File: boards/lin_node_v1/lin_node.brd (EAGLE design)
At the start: 50.1 x 38.4 mm, 27 parts, among them J1 AVR_SPI_PRG_6NS, U1 ATtiny167, U2 MCP2025, U3 VNQ5160K

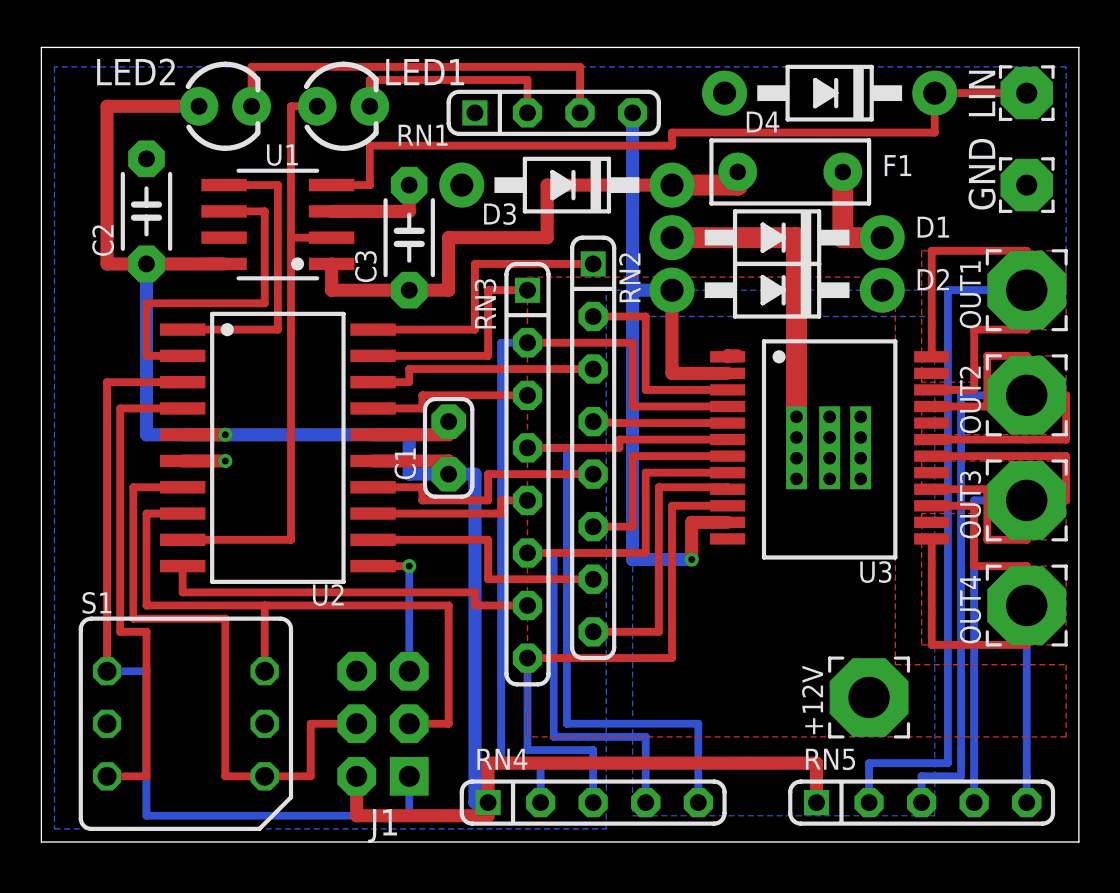
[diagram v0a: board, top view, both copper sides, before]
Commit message: Update to current sample boards
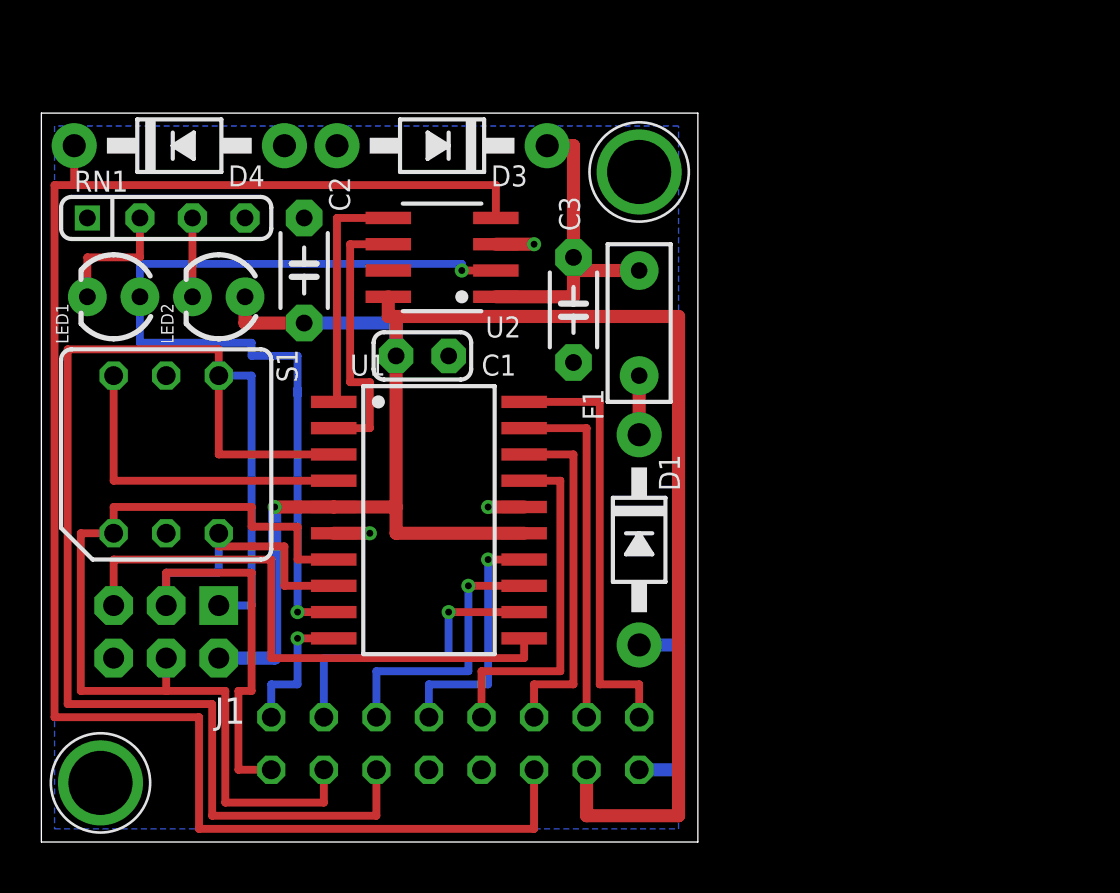
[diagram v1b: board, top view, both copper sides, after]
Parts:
- removed +12V, OUT1, OUT2, OUT3, OUT4: WIREPADTH-2.0MM, custom:WIREPAD-TH-2.0MM
- removed D2: 1N4004, custom:DO41-10
- removed GND, LIN: WIREPAD2,54/1,0, custom:2,54/1,0
- removed RN2, RN3: 10K, custom:SIL8
- removed RN4, RN5: 10K, custom:SIL5
- removed U3: VNQ5160K, custom:POWERSSO24
- added SV1: (no value), custom:FE08-2
- added U$1, U$2: MOUNT-HOLE3.1MM, custom:MOUNT-HOLE3.1
- moved D4 31.5 mm to (6.67, 33.7), turned to 0 degrees
- moved RN1 19.4 mm to (6.03, 30.2)
- moved D1 16.1 mm to (28.9, 14.6), turned to 270 degrees
- moved LED1 14.4 mm to (3.49, 26.4), turned to 180 degrees
- moved S1 13.1 mm to (6.03, 18.7), turned to 270 degrees
- moved J1 11.4 mm to (6.03, 10.2), turned to 180 degrees
- moved F1 10.3 mm to (28.9, 25.1), turned to 270 degrees
- moved LED2 9.21 mm to (8.57, 26.4), turned to 180 degrees
- moved C3 8.67 mm to (25.7, 25.7), turned to 270 degrees
- moved C2 8.14 mm to (12.7, 27.6)
- moved U1 8.09 mm to (18.7, 15.6)
- moved U2 8.09 mm to (19.4, 28.3)
- moved D3 6.33 mm to (19.4, 33.7)
- moved C1 4.62 mm to (18.4, 23.5), turned to 0 degrees
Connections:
- removed net N$1: D4.C, LIN.1, U2.4
- removed net N$10: RN3.2, RN4.2, U3.4
- removed net N$11: RN2.2, U3.3
- removed net N$12: RN2.8, U3.9
- removed net N$13: RN2.6, U3.7
- removed net N$14: RN2.4, U3.5
- removed net N$6: RN3.8, RN4.3, U3.10
- removed net N$7: RN3.6, RN4.4, U3.8
- removed net N$8: D2.A, RN1.4, U3.11, U3.2
- removed net N$9: RN3.4, RN4.5, U3.6
- removed net OUT1: RN2.1, U1.20
- removed net OUT2: RN2.3, U1.18
- removed net OUT3: RN2.5, U1.14
- removed net OUT4: RN2.7, U1.12
- removed net OUTPUT1: OUT1.1, RN5.2, U3.22, U3.23, U3.24
- removed net OUTPUT2: OUT2.1, RN5.3, U3.19, U3.20, U3.21
- removed net OUTPUT3: OUT3.1, RN5.4, U3.16, U3.17, U3.18
- removed net OUTPUT4: OUT4.1, RN5.5, U3.13, U3.14, U3.15
- removed net STATUS1: RN3.1, U1.19
- removed net STATUS2: RN3.3, U1.17
- removed net STATUS3: RN3.5, U1.13
- removed net STATUS4: RN3.7, U1.10
- new net LIN: D4.C, SV1.6, U2.4
- new net P0/SDA: SV1.1, U1.20
- new net P1: SV1.3, U1.19
- new net P2/SCL: SV1.5, U1.18
- new net P3: SV1.7, U1.17
- new net P4: SV1.9, U1.14
- new net P5/ADC8: SV1.11, U1.13
- new net P6/ADC9: SV1.13, U1.12
- new net P7/ADC7: SV1.15, U1.10
- net +12V: now also SV1.2; no longer +12V.1, U3.1, U3.12, U3.P$1, U3.P$10, U3.P$11, U3.P$12, U3.P$2, U3.P$3, U3.P$4, U3.P$5, U3.P$6, U3.P$7, U3.P$8, U3.P$9
- net +5V: now also SV1.4; no longer RN4.1, RN5.1
- net GND: now also SV1.10, SV1.8; no longer D2.C, GND.1
- net MISO: now also SV1.12
- net MOSI: now also SV1.14
- net SCK: now also SV1.16
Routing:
- net LIN: track 0.00 -> 82.0 mm
- net OUTPUT1: track 53.4 -> 0.00 mm
- net OUTPUT2: track 44.3 -> 0.00 mm
- net N$10: track 38.2 -> 0.00 mm
- net N$1: track 38.0 -> 0.00 mm
- net OUTPUT3: track 36.6 -> 0.00 mm
- net N$8: track 36.6 -> 0.00 mm, vias 1 -> 0
- net N$9: track 35.5 -> 0.00 mm
- net N$7: track 31.3 -> 0.00 mm
- net MISO: track 41.1 -> 71.9 mm
- net OUTPUT4: track 30.6 -> 0.00 mm
- net N$6: track 27.2 -> 0.00 mm
- net !RESET: track 6.83 -> 27.8 mm, vias 1 -> 0
- net P0/SDA: track 0.00 -> 20.8 mm
- net STATUS4: track 18.6 -> 0.00 mm
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- removed copper zone on layer 1, net +12V
- removed copper zone on layer 16, net +12V
- removed copper zone on layer 1, net OUTPUT1
- removed copper zone on layer 1, net OUTPUT2
- removed copper zone on layer 1, net OUTPUT3
- removed copper zone on layer 1, net OUTPUT4
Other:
- board size 50.1 x 38.4 mm -> 31.7 x 35.2 mm
- board text added: "12V"
- board text added: "5V"
- board text added: "GND"
- board text added: "LIN"
- board text added: "LIN slave controller v1 ©2014 michael smith"
- board text added: "MISO"
- board text added: "MOSI"
- board text added: "P0/SDA"
- board text added: "P1"
- board text added: "P2/SCL"
- board text added: "P3"
- board text added: "P4"
- board text added: "P5/ADC8"
- board text added: "P6/ADC9"
- board text added: "P7/ADC7"
- board text added: "SCK"
